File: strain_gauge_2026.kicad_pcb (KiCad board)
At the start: 2 copper layers, 30.2 x 17 mm, 0 parts

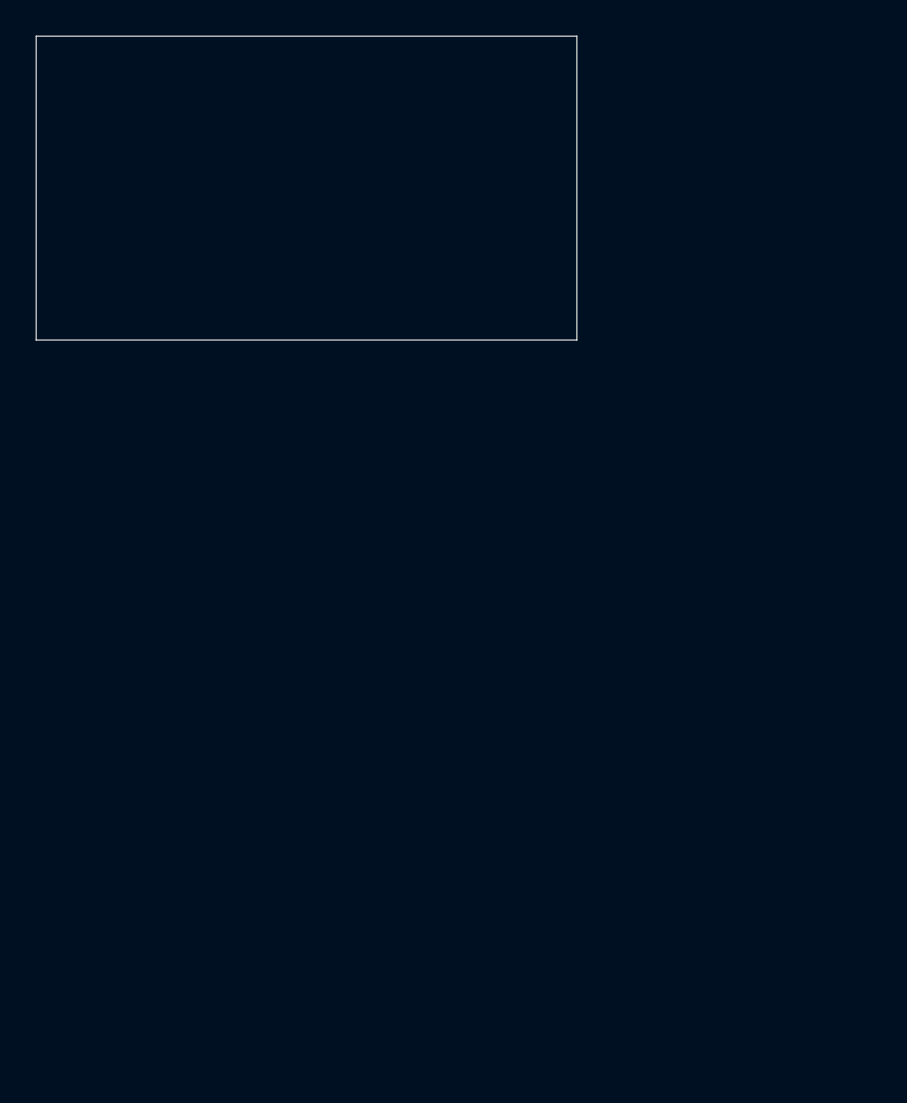
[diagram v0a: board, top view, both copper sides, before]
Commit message: Removed LTC4316 from schematic
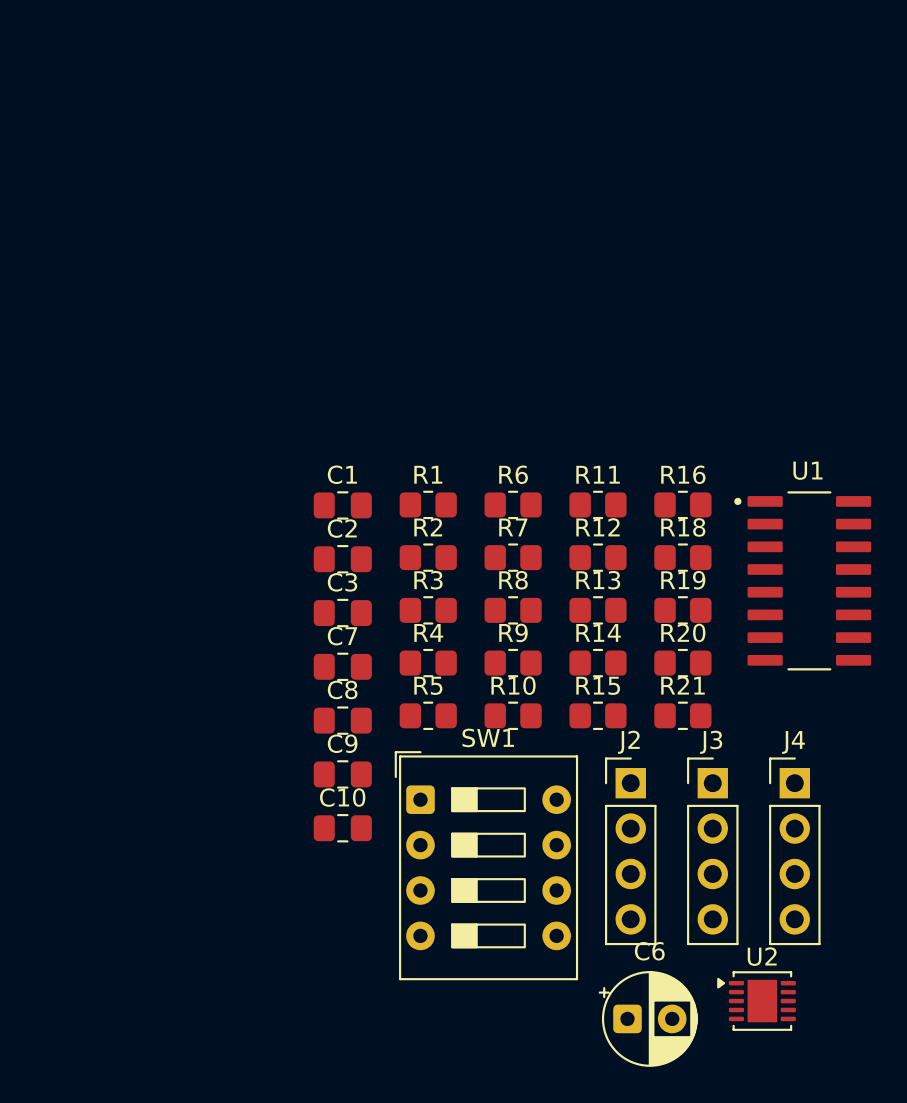
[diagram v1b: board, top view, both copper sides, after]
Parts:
- added C1: 0.1uF, Capacitor_SMD:C_0805_2012Metric_Pad1.18x1.45mm_HandSolder, F.Cu at (129.9, 94.5)
- added C10: 0.1uF, Capacitor_SMD:C_0805_2012Metric_Pad1.18x1.45mm_HandSolder, F.Cu at (129.9, 112.6)
- added C2: 0.1uF, Capacitor_SMD:C_0805_2012Metric_Pad1.18x1.45mm_HandSolder, F.Cu at (129.9, 97.5)
- added C3: 0.1uF, Capacitor_SMD:C_0805_2012Metric_Pad1.18x1.45mm_HandSolder, F.Cu at (129.9, 100.5)
- added C6: 10uF, Capacitor_THT:CP_Radial_D5.0mm_P2.50mm, F.Cu at (145.8, 123.2)
- added C7: 0.1uF, Capacitor_SMD:C_0805_2012Metric_Pad1.18x1.45mm_HandSolder, F.Cu at (129.9, 103.5)
- added C8: 0.1uF, Capacitor_SMD:C_0805_2012Metric_Pad1.18x1.45mm_HandSolder, F.Cu at (129.9, 106.5)
- added C9: 1uF, Capacitor_SMD:C_0805_2012Metric_Pad1.18x1.45mm_HandSolder, F.Cu at (129.9, 109.6)
- added J2: Conn_01x04_Socket, Connector_PinHeader_2.54mm:PinHeader_1x04_P2.54mm_Vertical, F.Cu at (146.0, 110.0)
- added J3: Conn_01x04_Socket, Connector_PinHeader_2.54mm:PinHeader_1x04_P2.54mm_Vertical, F.Cu at (150.6, 110.0)
- added J4: Conn_01x04_Socket, Connector_PinHeader_2.54mm:PinHeader_1x04_P2.54mm_Vertical, F.Cu at (155.2, 110.0)
- added R1: 10k, Resistor_SMD:R_0805_2012Metric_Pad1.20x1.40mm_HandSolder, F.Cu at (134.7, 94.5)
- added R10: 47, Resistor_SMD:R_0805_2012Metric_Pad1.20x1.40mm_HandSolder, F.Cu at (139.4, 106.3)
- added R11: 47, Resistor_SMD:R_0805_2012Metric_Pad1.20x1.40mm_HandSolder, F.Cu at (144.2, 94.5)
- added R12: 10k, Resistor_SMD:R_0805_2012Metric_Pad1.20x1.40mm_HandSolder, F.Cu at (144.2, 97.4)
- added R13: 681k, Resistor_SMD:R_0805_2012Metric_Pad1.20x1.40mm_HandSolder, F.Cu at (144.2, 100.4)
- added R14: 402k, Resistor_SMD:R_0805_2012Metric_Pad1.20x1.40mm_HandSolder, F.Cu at (144.2, 103.3)
- added R15: 604k, Resistor_SMD:R_0805_2012Metric_Pad1.20x1.40mm_HandSolder, F.Cu at (144.2, 106.3)
- added R16: 1.21M, Resistor_SMD:R_0805_2012Metric_Pad1.20x1.40mm_HandSolder, F.Cu at (148.9, 94.5)
- added R18: 1M, Resistor_SMD:R_0805_2012Metric_Pad1.20x1.40mm_HandSolder, F.Cu at (148.9, 97.4)
- added R19: 909k, Resistor_SMD:R_0805_2012Metric_Pad1.20x1.40mm_HandSolder, F.Cu at (148.9, 100.4)
- added R2: 350, Resistor_SMD:R_0805_2012Metric_Pad1.20x1.40mm_HandSolder, F.Cu at (134.7, 97.4)
- added R20: 100k, Resistor_SMD:R_0805_2012Metric_Pad1.20x1.40mm_HandSolder, F.Cu at (148.9, 103.3)
- added R21: 4.87M, Resistor_SMD:R_0805_2012Metric_Pad1.20x1.40mm_HandSolder, F.Cu at (148.9, 106.3)
- added R3: 350, Resistor_SMD:R_0805_2012Metric_Pad1.20x1.40mm_HandSolder, F.Cu at (134.7, 100.4)
- added R4: 350, Resistor_SMD:R_0805_2012Metric_Pad1.20x1.40mm_HandSolder, F.Cu at (134.7, 103.3)
- added R5: 350, Resistor_SMD:R_0805_2012Metric_Pad1.20x1.40mm_HandSolder, F.Cu at (134.7, 106.3)
- added R6: 350, Resistor_SMD:R_0805_2012Metric_Pad1.20x1.40mm_HandSolder, F.Cu at (139.4, 94.5)
- added R7: 350, Resistor_SMD:R_0805_2012Metric_Pad1.20x1.40mm_HandSolder, F.Cu at (139.4, 97.4)
- added R8: 47, Resistor_SMD:R_0805_2012Metric_Pad1.20x1.40mm_HandSolder, F.Cu at (139.4, 100.4)
- added R9: 47, Resistor_SMD:R_0805_2012Metric_Pad1.20x1.40mm_HandSolder, F.Cu at (139.4, 103.3)
- added SW1: SW_DIP_x04, Button_Switch_THT:SW_DIP_SPSTx04_Slide_9.78x12.34mm_W7.62mm_P2.54mm, F.Cu at (134.2, 111.0)
- added U1: NAU7802SGI, strain_gauge_footprint_lib:SOIC127P600X175-16N, F.Cu at (156.0, 98.7)
- added U2: LTC4316xDD, Package_DFN_QFN:DFN-10-1EP_3x3mm_P0.5mm_EP1.65x2.38mm, F.Cu at (153.4, 122.2)
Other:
- board outline removed

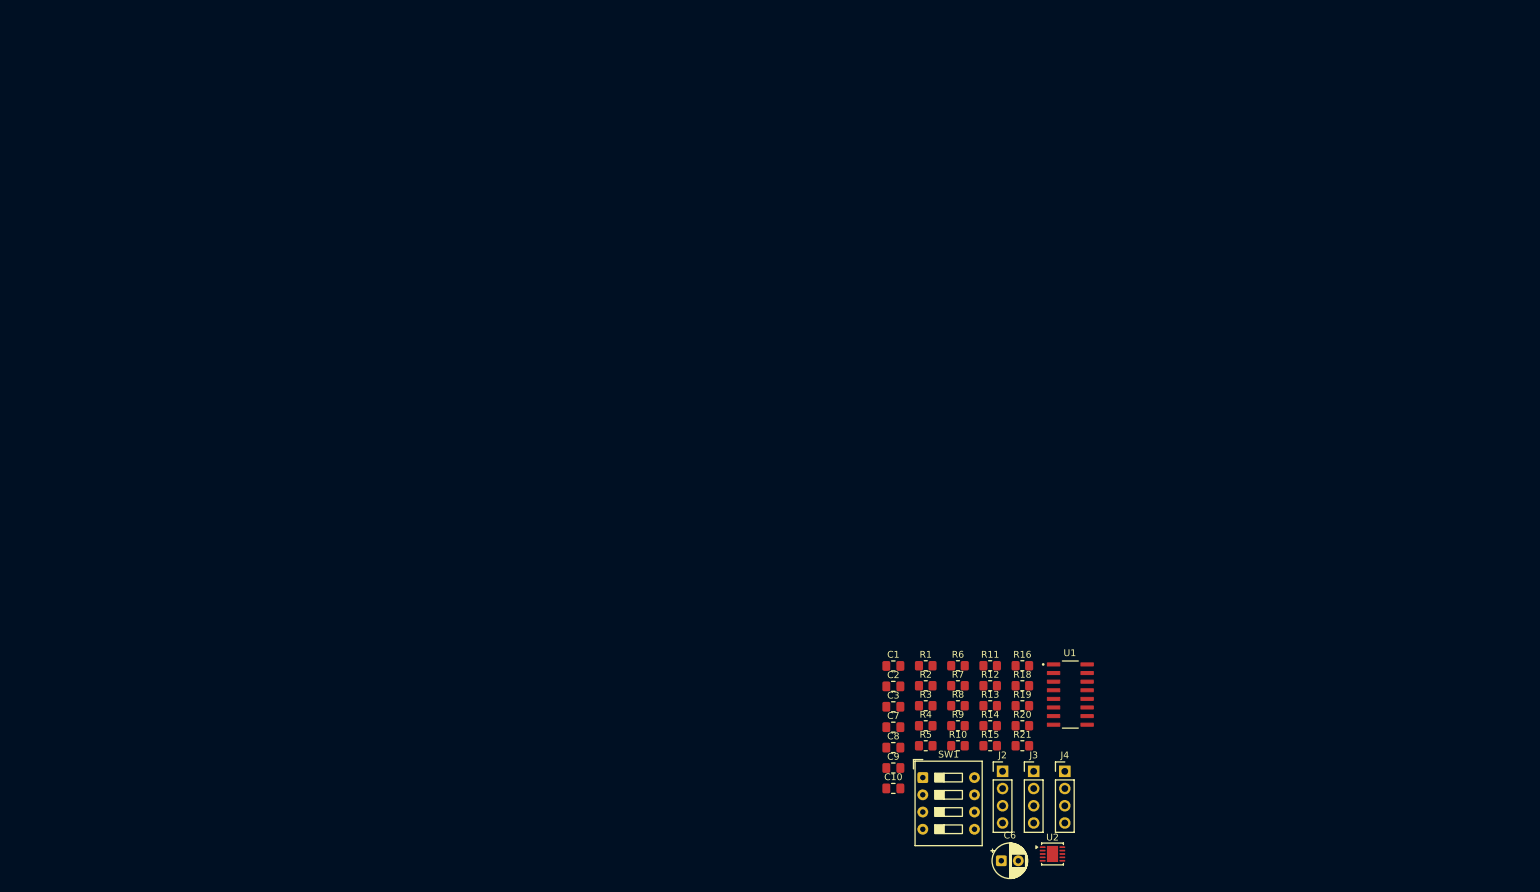
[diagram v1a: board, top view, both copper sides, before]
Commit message: Added optional Half/Quarter bridge connections
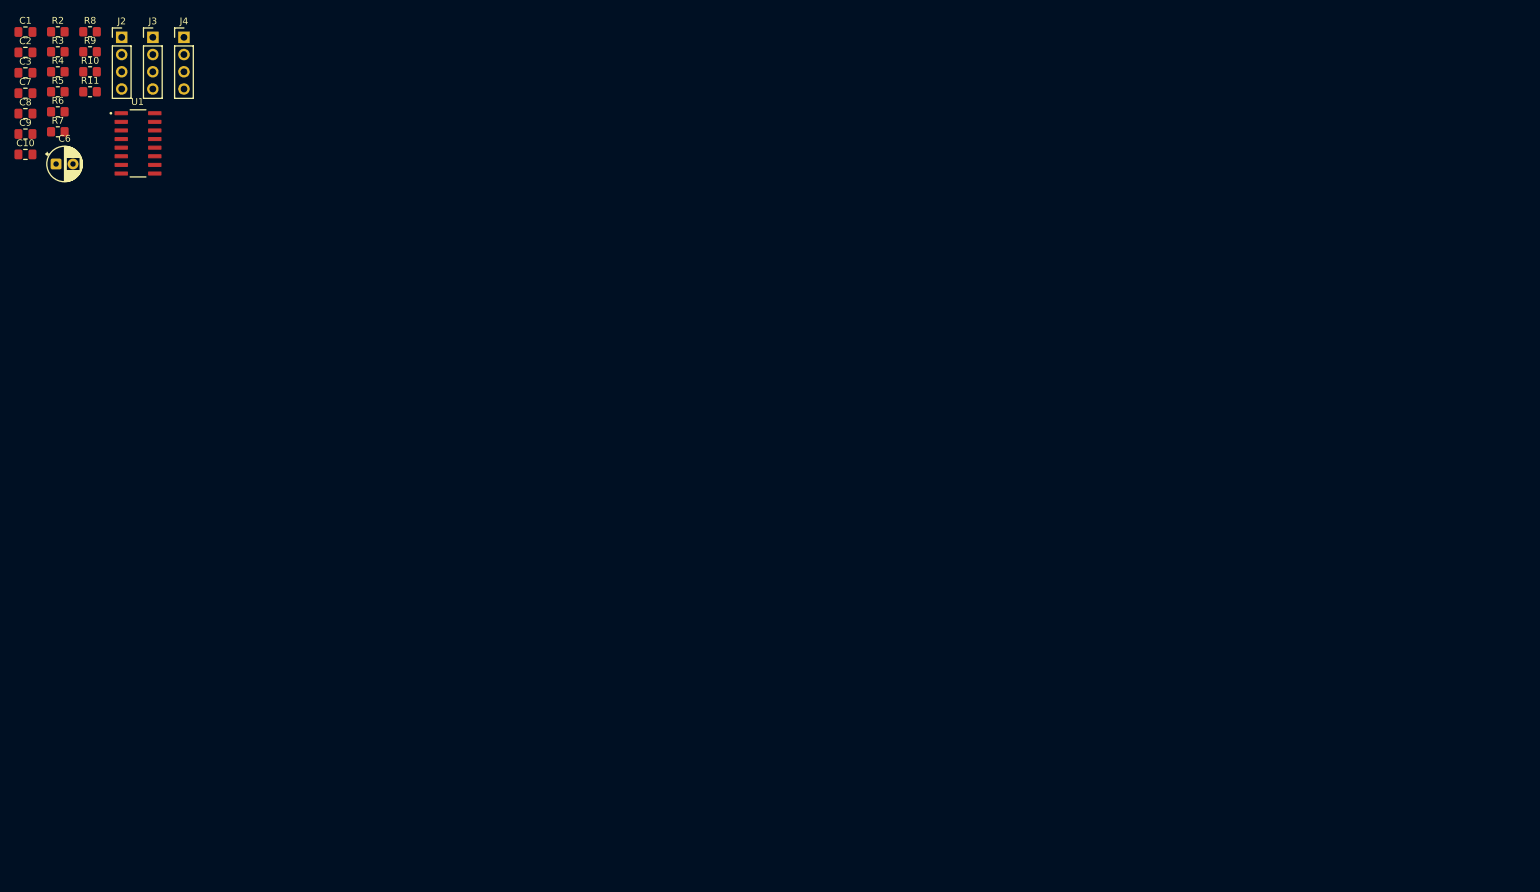
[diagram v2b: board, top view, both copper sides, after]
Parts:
- removed R1, R12: 10k, Resistor_SMD:R_0805_2012Metric_Pad1.20x1.40mm_HandSolder
- removed R13: 681k, Resistor_SMD:R_0805_2012Metric_Pad1.20x1.40mm_HandSolder
- removed R14: 402k, Resistor_SMD:R_0805_2012Metric_Pad1.20x1.40mm_HandSolder
- removed R15: 604k, Resistor_SMD:R_0805_2012Metric_Pad1.20x1.40mm_HandSolder
- removed R16: 1.21M, Resistor_SMD:R_0805_2012Metric_Pad1.20x1.40mm_HandSolder
- removed R18: 1M, Resistor_SMD:R_0805_2012Metric_Pad1.20x1.40mm_HandSolder
- removed R19: 909k, Resistor_SMD:R_0805_2012Metric_Pad1.20x1.40mm_HandSolder
- removed R20: 100k, Resistor_SMD:R_0805_2012Metric_Pad1.20x1.40mm_HandSolder
- removed R21: 4.87M, Resistor_SMD:R_0805_2012Metric_Pad1.20x1.40mm_HandSolder
- removed SW1: SW_DIP_x04, Button_Switch_THT:SW_DIP_SPSTx04_Slide_9.78x12.34mm_W7.62mm_P2.54mm
- removed U2: LTC4316xDD, Package_DFN_QFN:DFN-10-1EP_3x3mm_P0.5mm_EP1.65x2.38mm
- moved C6 173.2 mm to (6.42, 20.5)
- moved J2 169.1 mm to (16.1, 1.79)
- moved J3 169.1 mm to (20.7, 1.79)
- moved J4 169.1 mm to (25.3, 1.79)
- moved R10 162.1 mm to (11.4, 6.88)
- moved R8 162.1 mm to (11.4, 0.97)
- moved R9 162.1 mm to (11.4, 3.92)
- moved R2 160.3 mm to (6.68, 0.97)
- moved R3 160.3 mm to (6.68, 3.92)
- moved R4 160.3 mm to (6.68, 6.88)
- moved R5 160.3 mm to (6.68, 9.82)
- moved U1 159.7 mm to (18.5, 17.4)
- moved C1 158.5 mm to (1.91, 1.00)
- moved C10 158.5 mm to (1.91, 19.1)
- moved C2 158.5 mm to (1.91, 4.01)
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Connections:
- U1 pad 13: SCLK_ADC -> SCLK_MCU
- U1 pad 14: SDA_ADC -> SDA_MCU

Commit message: Passives selected, footprints assigned accordingly
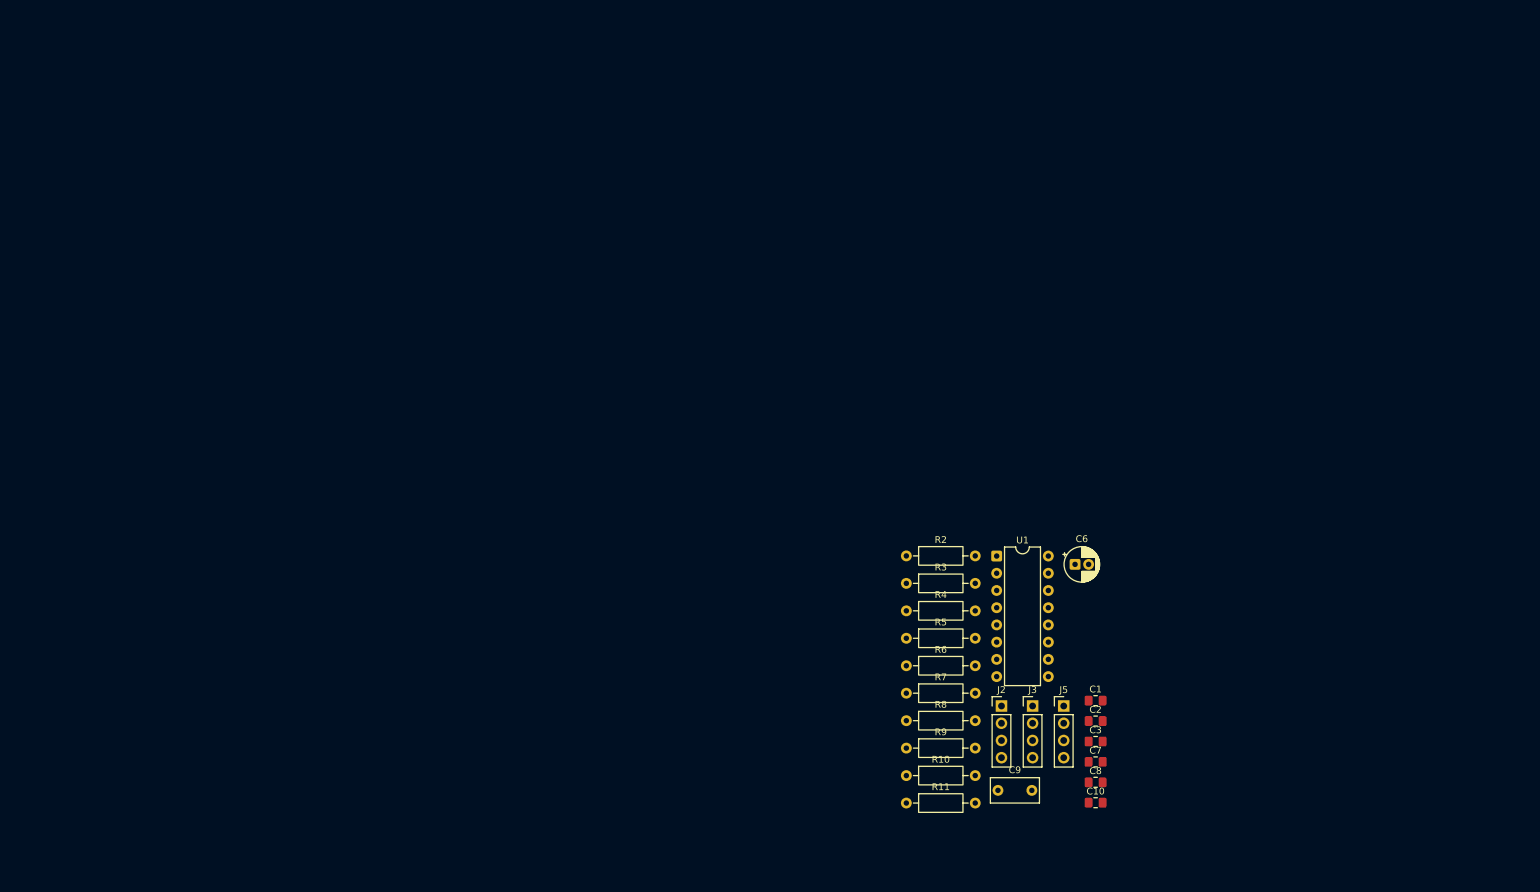
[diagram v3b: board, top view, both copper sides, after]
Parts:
- removed J4: Conn_01x04_Socket, Connector_PinHeader_2.54mm:PinHeader_1x04_P2.54mm_Vertical
- added J5: Conn_01x04_Socket, Connector_PinHeader_2.54mm:PinHeader_1x04_P2.54mm_Vertical, F.Cu at (155.0, 100.4)
- C6: footprint Capacitor_THT:CP_Radial_D5.0mm_P2.50mm -> Capacitor_THT:CP_Radial_D5.0mm_P2.00mm
- C9: footprint Capacitor_SMD:C_0805_2012Metric_Pad1.18x1.45mm_HandSolder -> Capacitor_THT:C_Rect_L7.0mm_W3.5mm_P5.00mm
- R10, R11, R2, R3, R4, R5, R6, R7, R8, R9: footprint Resistor_SMD:R_0805_2012Metric_Pad1.20x1.40mm_HandSolder -> Resistor_THT:R_Axial_DIN0207_L6.3mm_D2.5mm_P10.16mm_Horizontal
- U1: footprint strain_gauge_footprint_lib:SOIC127P600X175-16N -> Package_DIP:DIP-16_W7.62mm
- moved C1 186.1 mm to (159.7, 99.6)
- moved C2 186.1 mm to (159.7, 102.6)
- moved C3 186.1 mm to (159.7, 105.6)
- moved C7 186.1 mm to (159.7, 108.7)
- moved C8 186.1 mm to (159.7, 111.7)
- moved C10 184.5 mm to (159.7, 114.7)
- moved C9 173.0 mm to (145.3, 112.9)
- moved J2 163.0 mm to (145.9, 100.4)
- moved J3 163.0 mm to (150.4, 100.4)
- moved C6 161.5 mm to (156.7, 79.5)
- moved R11 159.7 mm to (131.8, 114.7)
- moved R10 159.0 mm to (131.8, 110.7)
- moved R9 158.2 mm to (131.8, 106.6)
- moved R8 157.5 mm to (131.8, 102.6)
- moved R7 150.1 mm to (131.8, 98.5)
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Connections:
- J3 pad 1: A+ -> V_excitation
- J3 pad 2: GND -> B+

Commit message: Initial PCB Layout
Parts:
- added REF**: MountingHole_2.2mm_M2_DIN965_Pad_TopBottom, MountingHole:MountingHole_2.2mm_M2_DIN965_Pad_TopBottom, F.Cu at (173.0, 116.0)
- added REF**: MountingHole_2.2mm_M2_DIN965_Pad_TopBottom, MountingHole:MountingHole_2.2mm_M2_DIN965_Pad_TopBottom, F.Cu at (117.5, 116.0)
- added REF**: MountingHole_2.2mm_M2_DIN965_Pad_TopBottom, MountingHole:MountingHole_2.2mm_M2_DIN965_Pad_TopBottom, F.Cu at (117.5, 81.5)
- added REF**: MountingHole_2.2mm_M2_DIN965_Pad_TopBottom, MountingHole:MountingHole_2.2mm_M2_DIN965_Pad_TopBottom, F.Cu at (173.0, 81.5)
- moved J5 36.0 mm to (121.5, 87.2)
- moved C6 33.3 mm to (167.5, 111.0), turned to 180 degrees
- moved J3 29.2 mm to (121.5, 104.0)
- moved C10 28.7 mm to (154.5, 86.5), turned to 90 degrees
- moved C9 28.3 mm to (158.0, 87.5)
- moved R9 24.9 mm to (142.9, 84.3), turned to -90 degrees
- moved R8 23.7 mm to (147.0, 84.3), turned to -90 degrees
- moved J2 23.3 mm to (169.0, 97.7)
- moved C8 21.3 mm to (169.0, 92.5), turned to 90 degrees
- moved R10 18.0 mm to (147.0, 100.9), turned to -90 degrees
- moved R6 18.0 mm to (137.6, 111.5), turned to 180 degrees
- moved R11 17.7 mm to (142.9, 100.9), turned to -90 degrees
- moved U1 17.6 mm to (153.9, 93.6)
- moved C7 17.3 mm to (166.0, 92.5), turned to 90 degrees
- moved C3 16.9 mm to (145.0, 114.0), turned to 180 degrees
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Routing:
- net V_excitation: track 0.00 -> 96.8 mm
- net B+: track 0.00 -> 35.1 mm
- net A+: track 0.00 -> 34.5 mm
- net +3V3: track 0.00 -> 30.6 mm
- net A-: track 0.00 -> 20.4 mm
- net B-: track 0.00 -> 20.4 mm
- net Net-(U1-VIN2N): track 0.00 -> 18.8 mm
- net Net-(U1-VIN1N): track 0.00 -> 16.5 mm
- net Net-(U1-VIN2P): track 0.00 -> 14.0 mm
- net Net-(U1-VIN1P): track 0.00 -> 12.6 mm
- net SDA_MCU: track 0.00 -> 8.29 mm
- net SCLK_MCU: track 0.00 -> 8.29 mm
- net Net-(U1-VBG): track 0.00 -> 6.43 mm
- added copper zone on F.Cu, net GND
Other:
- board outline added: 62.5 x 41.5 mm

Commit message: Added DFR1193 to Schematic and PCB Layout
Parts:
- added C6: 10uF, Capacitor_SMD:C_0805_2012Metric_Pad1.18x1.45mm_HandSolder, F.Cu at (211.2, 75.5)
- added C9: 1uF, Capacitor_SMD:C_0805_2012Metric_Pad1.18x1.45mm_HandSolder, F.Cu at (218.2, 75.2)
- added U2: ~, strain_gauge_footprint_lib:DFR1193, F.Cu at (205.2, 94.1)
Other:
- board text added: "New stuff"
- board text added: "TODO: J2 (4 pin connector) will be replaced with the 4 pin connector on the DFR1193 board. Also we updated all of the capacitors to be 0805 SMD, so those will need to be changed (C9 and C6). also make sure the track widths are 0.5mm minimum, i think thats the constraint for the Bechtel mill"
